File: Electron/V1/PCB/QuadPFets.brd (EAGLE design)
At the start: 99 x 40 mm, 53 parts, among them Q1 BC817-40SMD, Q2 BC817-40SMD, Q3 BC817-40SMD, Q4 BC817-40SMD, U1 MOSFET-PCHANNEL-SOIC8SOIC8, U2 MOSFET-PCHANNEL-SOIC8SOIC8, U3 MOSFET-PCHANNEL-SOIC8SOIC8, U4 MOSFET-PCHANNEL-SOIC8SOIC8, U5 ELECTRONDUALNAMED

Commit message: Moved LEDs to the top of the PCB so that components can be shifted left and make space between the FETs and the terminal block so that the channel id's can be shown next to the appropriate connection.
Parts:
- removed D10, D11, D7, D8, D9: (no value), SparkFun-DiscreteSemi:SOD-123
- added D101, D201, D301, D401: (no value), SparkFun-DiscreteSemi:SOD-123
- added FRAME2: FRAME-LETTER, SparkFun-Aesthetics:CREATIVE_COMMONS
- moved D1 27.2 mm to (74.3, 28.9), turned to 90 degrees
- moved R104 24.6 mm to (74.3, 24.4), turned to 90 degrees
- moved D2 20.8 mm to (77.5, 28.9), turned to 90 degrees
- moved R204 17.8 mm to (77.5, 24.4), turned to 90 degrees
- moved D3 14.3 mm to (80.6, 28.9), turned to 90 degrees
- moved R304 10.7 mm to (80.6, 24.4), turned to 90 degrees
- moved D4 8.98 mm to (83.7, 28.9), turned to 90 degrees
- moved Q3 5.24 mm to (85.1, 15.2)
- moved Q1 5.08 mm to (85.1, 3.81)
- moved Q2 5.08 mm to (85.1, 10.2)
- moved R303 4.62 mm to (80.3, 16.1)
- moved R403 4.45 mm to (84.8, 19.3)
- moved R103 4.44 mm to (80.3, 5.08)
- moved R203 4.44 mm to (80.3, 11.1)
- moved R404 3.73 mm to (83.7, 24.4), turned to 90 degrees
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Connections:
- net CHANNEL_1_FEED: now also D101.C; no longer D9.C
- net CHANNEL_2_FEED: now also D201.C; no longer D10.C
- net CHANNEL_3_FEED: now also D301.C; no longer D8.C
- net CHANNEL_4_FEED: now also D401.C; no longer D7.C
- net GND: now also D101.A, D201.A, D301.A, D401.A; no longer D10.A, D7.A, D8.A, D9.A
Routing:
- net CHANNEL_2: track 67.4 -> 77.6 mm, vias 4 -> 6
- net CHANNEL_4: track 83.0 -> 78.0 mm
- net CHANNEL_1_FEED: track 13.8 -> 18.0 mm
- net CHANNEL_1: track 74.8 -> 70.7 mm, vias 2 -> 4
- net N$22: track 5.94 -> 9.90 mm
- net N$3: track 5.94 -> 8.48 mm
- net CHANNEL_3: track 90.8 -> 93.1 mm, vias 2 -> 4
- net N$4: track 5.94 -> 8.09 mm
- net CHANNEL_4_FEED: track 44.7 -> 46.6 mm
- net CHANNEL_2_FEED: track 30.6 -> 32.6 mm
- net CHANNEL_3_FEED: track 36.7 -> 38.6 mm
- net N$57: track 4.09 -> 2.81 mm
- net N$55: track 4.04 -> 5.17 mm
- net VIN: track 13.7 -> 14.6 mm
- net N$13: track 3.53 -> 2.81 mm
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
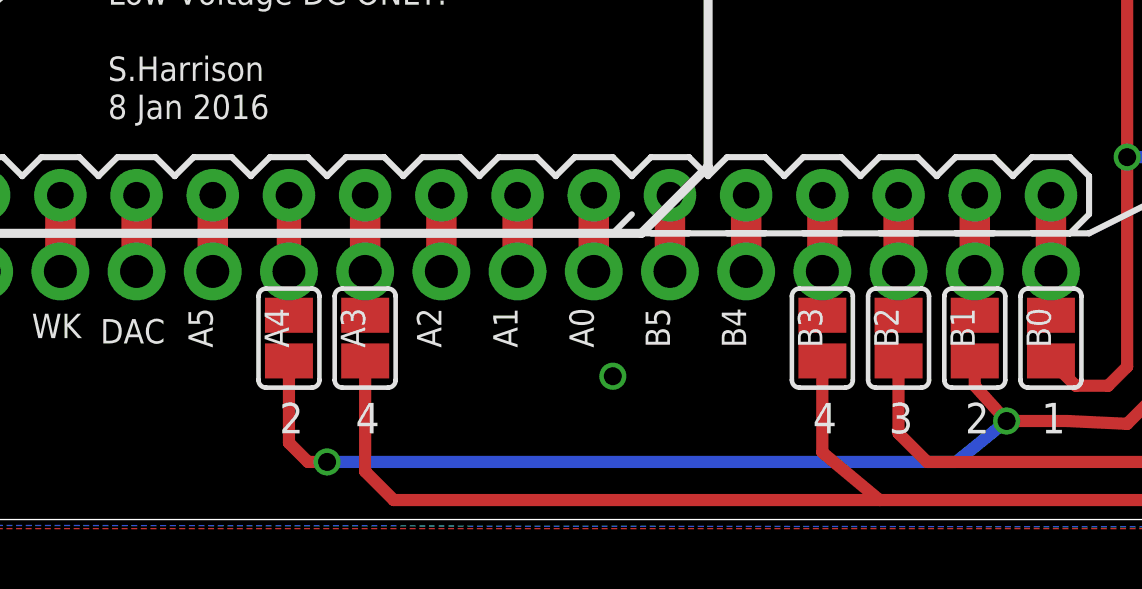
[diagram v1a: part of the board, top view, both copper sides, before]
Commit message: Update to swap channel 4 onto A5 rather than A3 as A3 does not support PWM.
DirtyPCBs order updated.
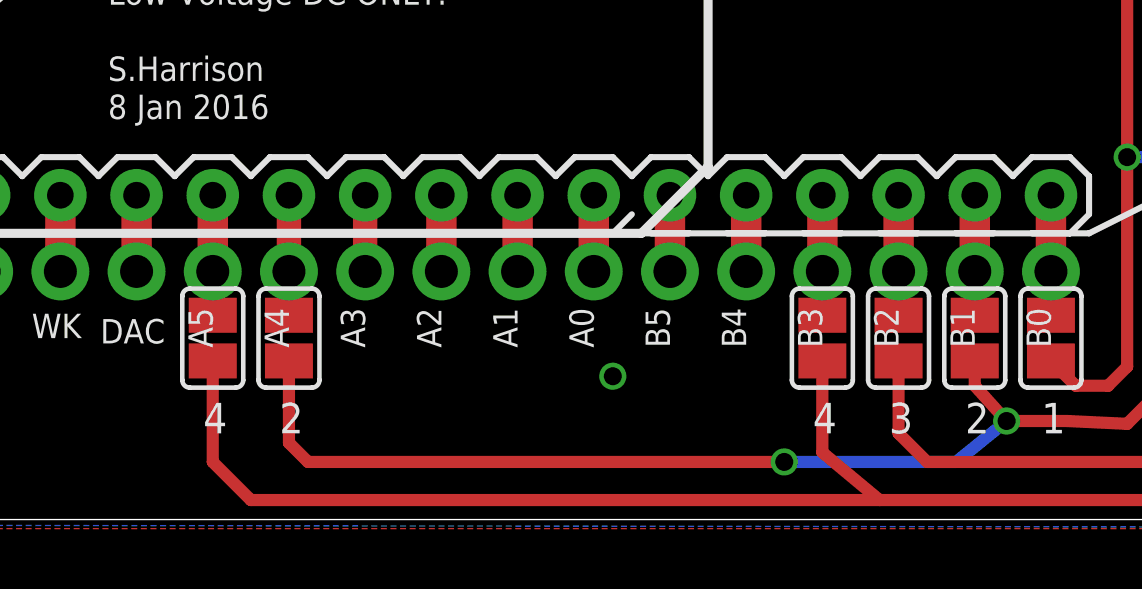
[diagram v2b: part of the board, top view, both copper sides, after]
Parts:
- removed SJ7: (no value), jumper:SJ
- added SJ9: (no value), jumper:SJ
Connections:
- net CHANNEL_4: now also SJ9.1; no longer SJ7.1
- net N$42: no longer SJ7.2
- net N$44: now also SJ9.2
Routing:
- net CHANNEL_4: track 78.0 -> 82.9 mm
- net N$44: track 2.54 -> 4.00 mm
- net N$42: track 4.00 -> 2.54 mm
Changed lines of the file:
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@@
 <setting verticaltext="up"/>
 </settings>
-<grid distance="0.025" unitdist="inch" unit="mm" style="lines" multiple="1" display="yes" altdistance="0.0125" altunitdist="inch" altunit="inch"/>
+<grid distance="0.025" unitdist="inch" unit="inch" style="lines" multiple="1" display="yes" altdistance="0.0125" altunitdist="inch" altunit="inch"/>
 <layers>
 <layer number="1" name="Top" color="4" fill="1" visible="yes" active="yes"/>
@@
 <dimension x1="15" y1="-3.5" x2="114" y2="1" x3="64.5" y3="39.65" textsize="1.27" layer="47" dtype="horizontal"/>
 <text x="70.8025" y="27.6225" size="2.54" layer="25" font="vector">1</text>
-<text x="43.4975" y="-4.1275" size="1.016" layer="25" font="vector">4</text>
+<text x="38.4175" y="-4.1275" size="1.016" layer="25" font="vector">4</text>
 <text x="58.7375" y="-4.1275" size="1.016" layer="25" font="vector">4</text>
 <text x="61.2775" y="-4.1275" size="1.016" layer="25" font="vector">3</text>
@@
 <attribute name="VALUE" x="43.815" y="27.0701" size="0.02" layer="27" rot="R90"/>
 </element>
-<element name="SJ7" library="jumper" package="SJ" value="" x="43.815" y="-0.9525" smashed="yes" rot="R90">
-<attribute name="VALUE" x="43.815" y="-0.5524" size="0.02" layer="27" rot="R90"/>
-</element>
 <element name="SJ8" library="jumper" package="SJ" value="" x="41.275" y="-0.9525" smashed="yes" rot="R90">
 <attribute name="VALUE" x="41.275" y="-0.5524" size="0.02" layer="27" rot="R90"/>
@@
 </element>
 <element name="FRAME2" library="SparkFun-Aesthetics" package="CREATIVE_COMMONS" value="FRAME-LETTER" x="13.335" y="-15.24"/>
+<element name="SJ9" library="jumper" package="SJ" value="" x="38.735" y="-0.9525" smashed="yes" rot="R90">
+<attribute name="VALUE" x="38.735" y="-0.5524" size="0.02" layer="27" rot="R90"/>
+</element>
 </elements>
 <signals>
@@
 <wire x1="46.355" y1="1.27" x2="46.355" y2="3.81" width="1.016" layer="1"/>
 </signal>
-<signal name="N$42">
-<contactref element="U5" pad="A3"/>
-<contactref element="U5" pad="A3_1"/>
-<wire x1="43.815" y1="3.81" x2="43.815" y2="1.27" width="1.016" layer="1"/>
-<contactref element="SJ7" pad="2"/>
-<wire x1="43.815" y1="-0.1905" x2="43.815" y2="1.27" width="0.4064" layer="1"/>
-</signal>
 <signal name="N$44">
 <contactref element="U5" pad="A5"/>
 <contactref element="U5" pad="A5_1"/>
 <wire x1="38.735" y1="3.81" x2="38.735" y2="1.27" width="1.016" layer="1"/>
+<contactref element="SJ9" pad="2"/>
+<wire x1="38.735" y1="-0.1905" x2="38.735" y2="1.27" width="0.8128" layer="1"/>
 </signal>
 <signal name="N$45">
@@
 <wire x1="41.275" y1="-1.7145" x2="41.275" y2="-4.445" width="0.4064" layer="1"/>
 <wire x1="41.275" y1="-4.445" x2="41.91" y2="-5.08" width="0.4064" layer="1"/>
-<wire x1="41.91" y1="-5.08" x2="42.545" y2="-5.08" width="0.4064" layer="1"/>
-<via x="42.545" y="-5.08" extent="1-16" drill="0.6"/>
-<wire x1="42.545" y1="-5.08" x2="63.514503125" y2="-5.08" width="0.4064" layer="16"/>
+<wire x1="41.91" y1="-5.08" x2="57.785" y2="-5.08" width="0.4064" layer="1"/>
+<via x="57.785" y="-5.08" extent="1-16" drill="0.6"/>
+<wire x1="57.785" y1="-5.08" x2="63.514503125" y2="-5.08" width="0.4064" layer="16"/>
 <wire x1="63.514503125" y1="-5.08" x2="65.1962875" y2="-3.715715625" width="0.4064" layer="16"/>
 <via x="65.1962875" y="-3.715715625" extent="1-16" drill="0.6"/>
@@
 </signal>
 <signal name="CHANNEL_4">
-<contactref element="SJ7" pad="1"/>
 <contactref element="SJ1" pad="1"/>
 <wire x1="73.025" y1="-4.445" x2="71.12" y2="-6.35" width="0.4064" layer="1"/>
 <wire x1="71.12" y1="-6.35" x2="60.96" y2="-6.35" width="0.4064" layer="1"/>
-<wire x1="44.7675" y1="-6.35" x2="43.815" y2="-5.3975" width="0.4064" layer="1"/>
-<wire x1="43.815" y1="-5.3975" x2="43.815" y2="-1.7145" width="0.4064" layer="1"/>
-<wire x1="44.7675" y1="-6.35" x2="60.96" y2="-6.35" width="0.4064" layer="1"/>
+<wire x1="40.005" y1="-6.35" x2="60.96" y2="-6.35" width="0.4064" layer="1"/>
 <wire x1="60.96" y1="-6.35" x2="59.055" y2="-4.7625" width="0.4064" layer="1"/>
 <wire x1="59.055" y1="-4.7625" x2="59.055" y2="-1.7145" width="0.4064" layer="1"/>
@@
 <wire x1="83.82" y1="22.225" x2="83.82" y2="23.46" width="0.4064" layer="1"/>
 <wire x1="83.82" y1="23.46" x2="83.7325" y2="23.5475" width="0.4064" layer="1"/>
+<contactref element="SJ9" pad="1"/>
+<wire x1="40.005" y1="-6.35" x2="38.735" y2="-5.08" width="0.4064" layer="1"/>
+<wire x1="38.735" y1="-5.08" x2="38.735" y2="-1.7145" width="0.4064" layer="1"/>
 </signal>
 <signal name="CHANNEL_3">
@@
 <wire x1="83.7325" y1="27.3925" x2="83.7325" y2="25.3475" width="0.4064" layer="1"/>
 </signal>
+<signal name="N$42">
+<contactref element="U5" pad="A3_1"/>
+<contactref element="U5" pad="A3"/>
+<wire x1="43.815" y1="3.81" x2="43.815" y2="1.27" width="0.8128" layer="1"/>
+</signal>
 </signals>
